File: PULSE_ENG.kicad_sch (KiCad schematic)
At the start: 14 parts, among them IC27 ADM3071EARZ, J1 TC2030-MCP, J2 G125-FV10805F3-1AB1ABP, J3 G125-FV10805F3-1AB1ABP, J4 G125-FV10805F3-1AB1ABP, J6 G125-FV10805F3-1AB1ABP, J7 12401832E402A, U1 ATSAMD21J17D-M

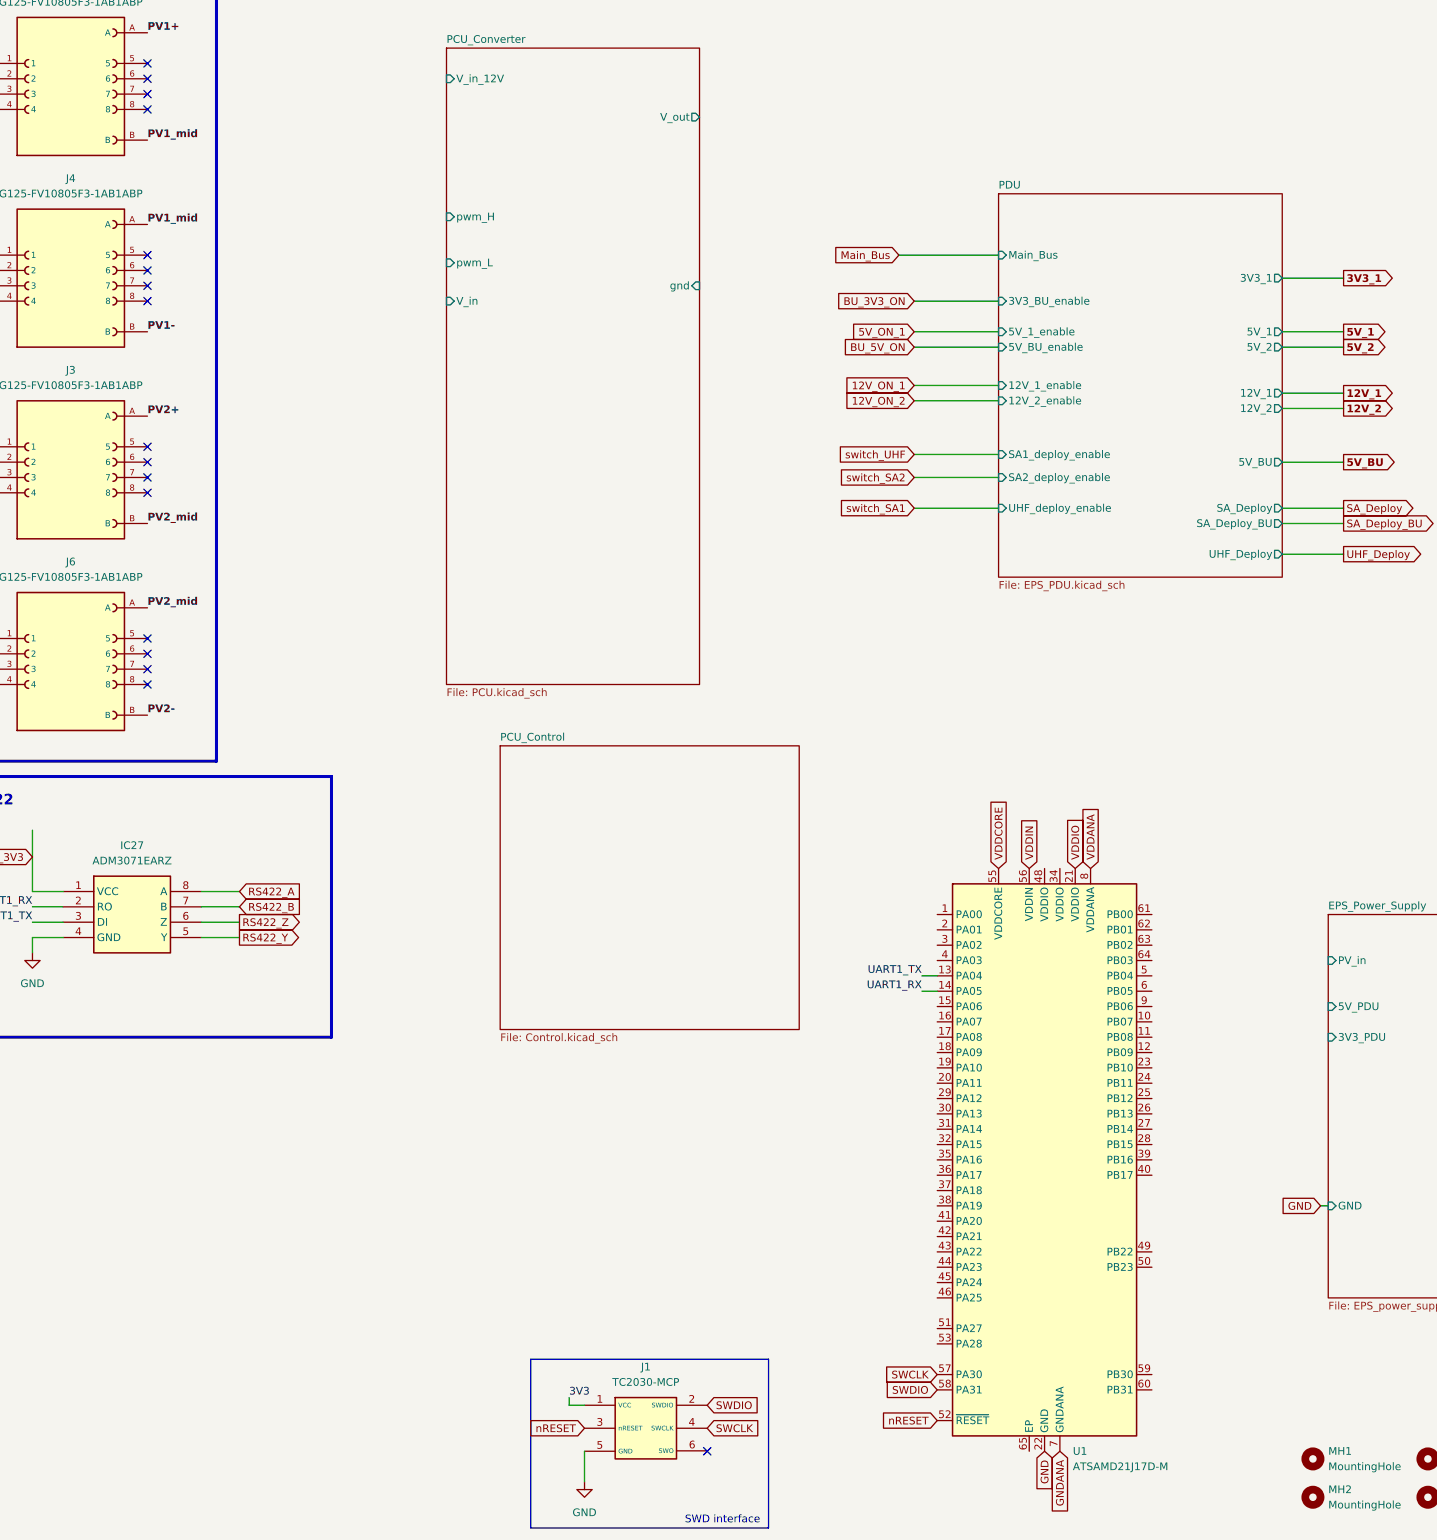
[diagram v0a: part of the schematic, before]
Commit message: Created a page for BAT eFuse and current sensing. Updated the cControl page with part of the harware cutoff
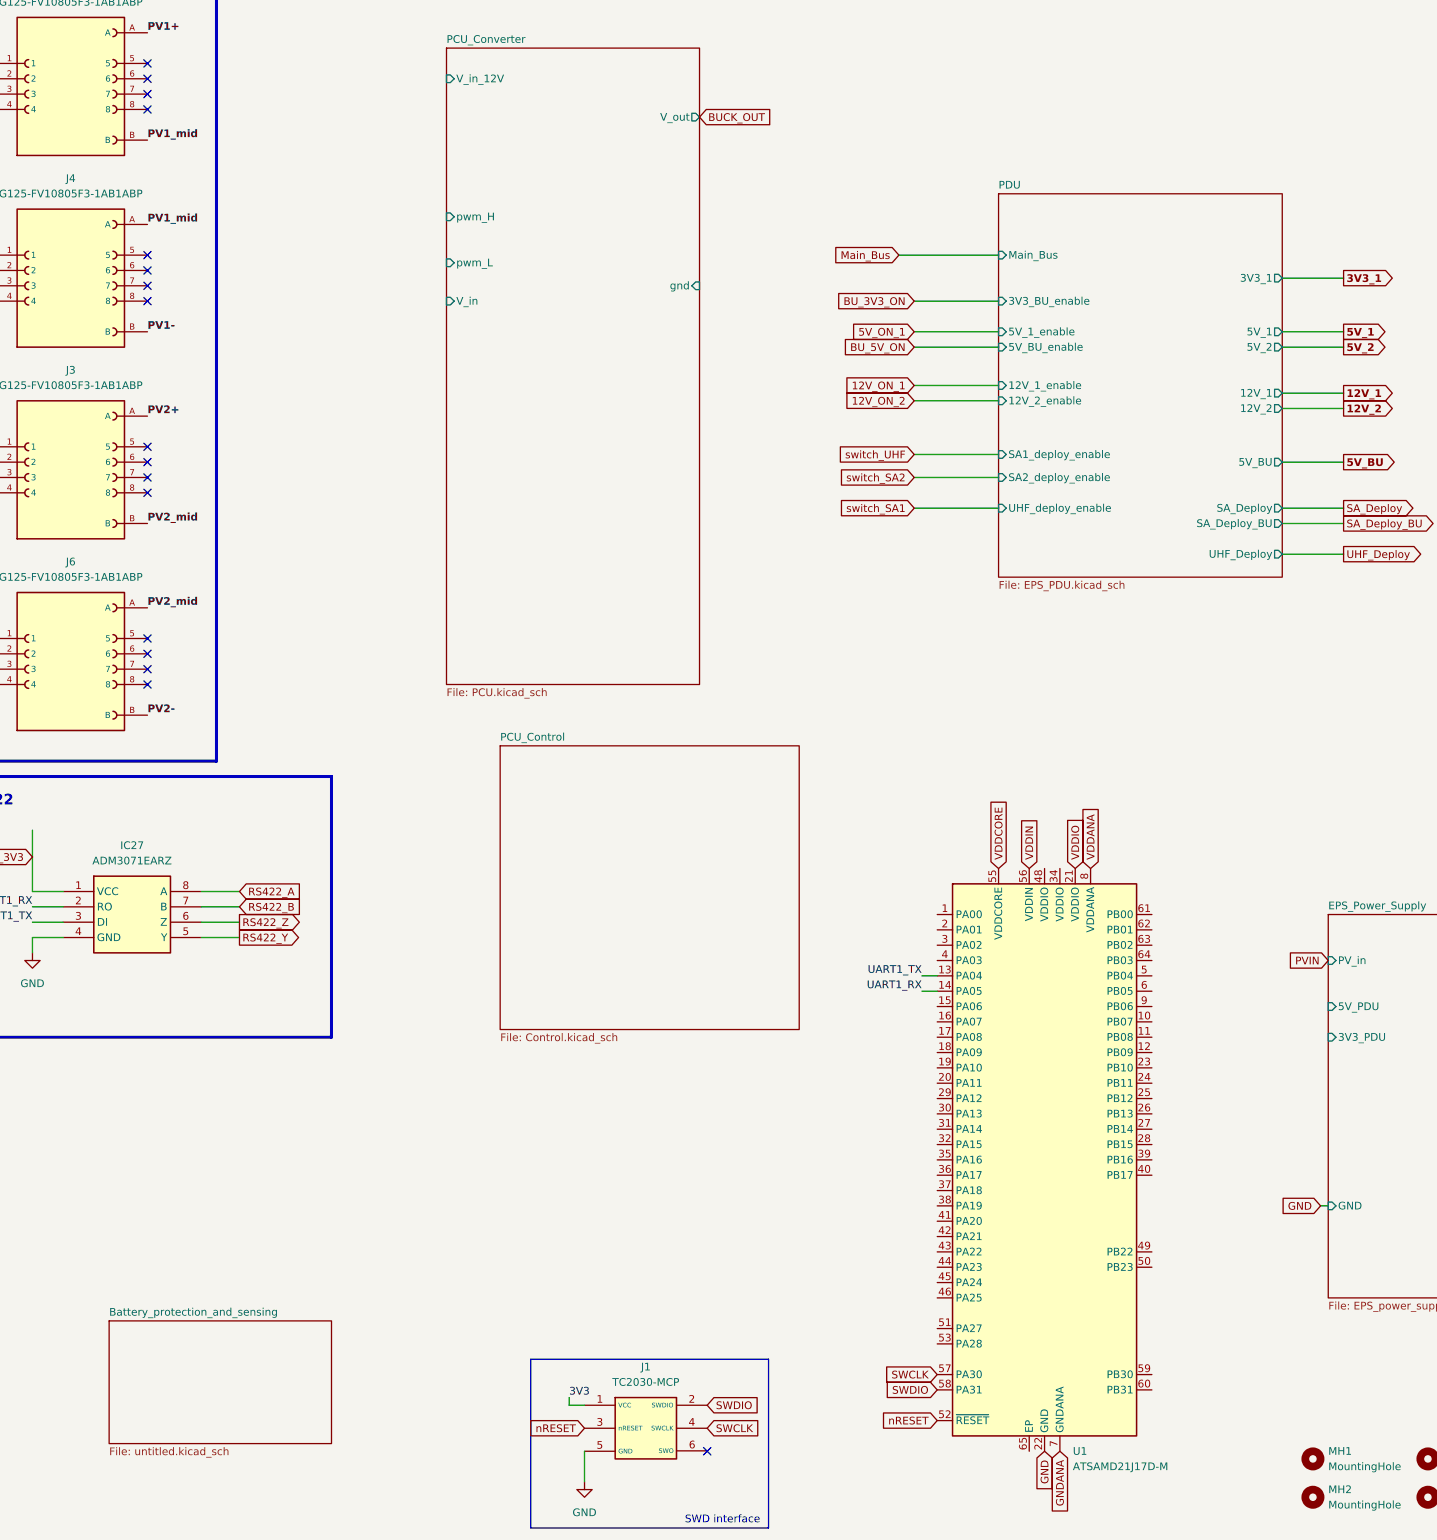
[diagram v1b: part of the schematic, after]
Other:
- added sheet Battery_protection_and_sensing (untitled.kicad_sch)
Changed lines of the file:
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@@
 		)
 	)
+	(global_label "BUCK_OUT"
+		(shape input)
+		(at 138.43 44.45 0)
+		(fields_autoplaced yes)
+		(effects
+			(font
+				(size 1.27 1.27)
+			)
+			(justify left)
+		)
+		(property "Intersheetrefs" "${INTERSHEET_REFS}"
+			(at 151.1519 44.45 0)
+			(effects
+				(font
+					(size 1.27 1.27)
+				)
+				(justify left)
+				(hide yes)
+			)
+		)
+	)
 	(global_label "BU_Vbat_ON"
 		(shape output)
@@
 		)
 	)
+	(global_label "PVIN"
+		(shape input)
+		(at 242.57 184.15 180)
+		(fields_autoplaced yes)
+		(effects
+			(font
+				(size 1.27 1.27)
+			)
+			(justify right)
+		)
+		(property "Intersheetrefs" "${INTERSHEET_REFS}"
+			(at 235.2909 184.15 0)
+			(effects
+				(font
+					(size 1.27 1.27)
+				)
+				(justify right)
+				(hide yes)
+			)
+		)
+	)
 	(global_label "BU_3V3_ON"
 		(shape input)
@@
 				)
 			)
+		)
+	)
+	(sheet
+		(at 40.64 243.84)
+		(size 36.83 20.32)
+		(exclude_from_sim no)
+		(in_bom yes)
+		(on_board yes)
+		(dnp no)
+		(fields_autoplaced yes)
+		(stroke
+			(width 0.1524)
+			(type solid)
+		)
+		(fill
+			(color 0 0 0 0.0000)
+		)
+		(property "Sheetname" "Battery_protection_and_sensing"
+			(at 40.64 243.1284 0)
+			(effects
+				(font
+					(size 1.27 1.27)
+				)
+				(justify left bottom)
+			)
+		)
+		(property "Sheetfile" "untitled.kicad_sch"
+			(at 40.64 264.7446 0)
+			(effects
+				(font
+					(size 1.27 1.27)
+				)
+				(justify left top)
+			)
+		)
+		(instances
+			(project "PULSE_ENG"
+				(path "/2de881bb-2e2a-47f9-96ed-b3393fa36b98"
+					(page "6")
+				)
+			)

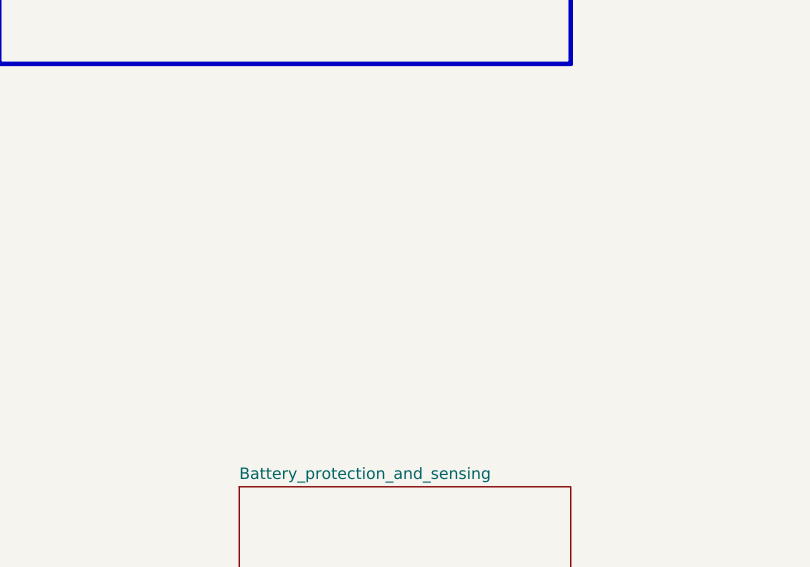
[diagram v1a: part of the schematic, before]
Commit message: Created a page for PANNEL efuse, modifiel all to local labels, functionally finished
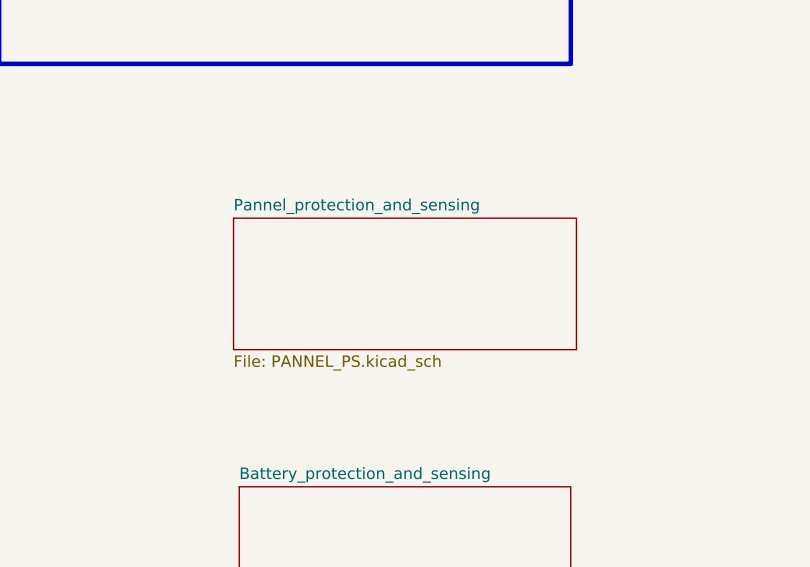
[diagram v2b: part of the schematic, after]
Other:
- added sheet Pannel_protection_and_sensing (PANNEL_PS.kicad_sch)
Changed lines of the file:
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@@
+		)
+	)
+	(sheet
+		(at 40.005 213.995)
+		(size 38.1 14.605)
+		(exclude_from_sim no)
+		(in_bom yes)
+		(on_board yes)
+		(dnp no)
+		(fields_autoplaced yes)
+		(stroke
+			(width 0.1524)
+			(type solid)
+		)
+		(fill
+			(color 0 0 0 0.0000)
+		)
+		(property "Sheetname" "Pannel_protection_and_sensing"
+			(at 40.005 213.2834 0)
+			(effects
+				(font
+					(size 1.27 1.27)
+				)
+				(justify left bottom)
+			)
+		)
+		(property "Sheetfile" "PANNEL_PS.kicad_sch"
+			(at 40.005 229.1846 0)
+			(effects
+				(font
+					(size 1.27 1.27)
+				)
+				(justify left top)
+			)
+		)
+		(instances
+			(project "PULSE_ENG"
+				(path "/2de881bb-2e2a-47f9-96ed-b3393fa36b98"
+					(page "7")
+				)
+			)
 		)
 	)

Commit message: Some edits
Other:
- sheet Battery_protection_and_sensing ports: added 3.3V, 5V, BAT_EFUSE_EN, BAT_EFUSE_FLT, BAT_EFUSE_IMON, BAT_EFUSE_PGOOD, BAT_HS, BAT_NEG, BAT_POS, BAT_PS, BAT_SHUNT_IN, BAT_SHUNT_OUT, BAT_VCC, BUCK_OUT, GND, P_SYS_Protected; removed none
- sheet PCU_Control ports: added 3.3V, 5V, BAT_EFUSE_EN, BAT_OVP_FLAG, BAT_SHUNT_IN, BAT_SHUNT_OUT, BAT_UVP_FLAG, BUCK_IN, BUCK_OUT, I_BAT_ANA, I_PANNEL_ANA, MCU_BAT_EFUSE_EN, MCU_PANNEL_EFUSE_EN, PANNEL_EFUSE_EN, PANNEL_OVP_FLAG, PANNEL_SHUNT_IN, PANNEL_SHUNT_OUT, P_SYS_Protected, VBAT_SENSE, VPANNEL_SENSE; removed none
- sheet Pannel_protection_and_sensing ports: added 3.3V, 5V, PANNEL_EFUSE_EN, PANNEL_SHUNT_IN, PANNEL_SHUNT_OUT, PAN_EFUSE_FLT, PAN_EFUSE_IMON, PAN_EFUSE_PGOOD, P_Vout_PROTECTED, Vin_PANNEL; removed none

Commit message: Modification of ROOT sheet blocks
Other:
- moved on the sheet: H1, H2, J1, J7, MH1, MH2, MH3, MH4, U1
